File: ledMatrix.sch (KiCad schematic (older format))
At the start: 21 parts

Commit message: BIG UPDATE! omg so big
New boards and other things.. jeesh it sbeen too long since the last update
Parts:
- LED1, LED10, LED11, LED12, LED13, LED14, LED15, LED16, LED2, LED3, LED4, LED5, LED6, LED7, LED8, LED9: footprint afx-01:WS2811_5mm_ThroughHole -> Zetaohm:WS2812b_SMD
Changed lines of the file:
@@
 EESchema Schematic File Version 2
-LIBS:afx-01-rescue
+LIBS:Zetaohm
 LIBS:power
 LIBS:device
@@
 LIBS:contrib
 LIBS:valves
-LIBS:afx-01-cache
-LIBS:ZettaOhm
 EELAYER 25 0
 EELAYER END
 $Descr User 5906 5906
 encoding utf-8
-Sheet 2 5
+Sheet 2 7
 Title ""
 Date ""
@@
 F 0 "LED1" H 2750 1750 20  0000 C CNN
 F 1 "WS2812b" H 2600 1750 20  0000 C CNN
-F 2 "afx-01:WS2811_5mm_ThroughHole" H 2300 2250 60  0001 C CNN
+F 2 "Zetaohm:WS2812b_SMD" H 2300 2250 60  0001 C CNN
 F 3 "" H 2300 2250 60  0000 C CNN
 	1    2600 1500
@@
 F 0 "LED5" H 2750 2300 20  0000 C CNN
 F 1 "WS2812b" H 2600 2300 20  0000 C CNN
-F 2 "afx-01:WS2811_5mm_ThroughHole" H 2300 2800 60  0001 C CNN
+F 2 "Zetaohm:WS2812b_SMD" H 2300 2800 60  0001 C CNN
 F 3 "" H 2300 2800 60  0000 C CNN
 	1    2600 2050
@@
 F 0 "LED9" H 2750 2850 20  0000 C CNN
 F 1 "WS2812b" H 2600 2850 20  0000 C CNN
-F 2 "afx-01:WS2811_5mm_ThroughHole" H 2300 3350 60  0001 C CNN
+F 2 "Zetaohm:WS2812b_SMD" H 2300 3350 60  0001 C CNN
 F 3 "" H 2300 3350 60  0000 C CNN
 	1    2600 2600
@@
 F 0 "LED13" H 2750 3400 20  0000 C CNN
 F 1 "WS2812b" H 2600 3400 20  0000 C CNN
-F 2 "afx-01:WS2811_5mm_ThroughHole" H 2300 3900 60  0001 C CNN
+F 2 "Zetaohm:WS2812b_SMD" H 2300 3900 60  0001 C CNN
 F 3 "" H 2300 3900 60  0000 C CNN
 	1    2600 3150
@@
 F 0 "LED2" H 3250 1750 20  0000 C CNN
 F 1 "WS2812b" H 3100 1750 20  0000 C CNN
-F 2 "afx-01:WS2811_5mm_ThroughHole" H 2800 2250 60  0001 C CNN
+F 2 "Zetaohm:WS2812b_SMD" H 2800 2250 60  0001 C CNN
 F 3 "" H 2800 2250 60  0000 C CNN
 	1    3100 1500
@@
 F 0 "LED6" H 3250 2300 20  0000 C CNN
 F 1 "WS2812b" H 3100 2300 20  0000 C CNN
-F 2 "afx-01:WS2811_5mm_ThroughHole" H 2800 2800 60  0001 C CNN
+F 2 "Zetaohm:WS2812b_SMD" H 2800 2800 60  0001 C CNN
 F 3 "" H 2800 2800 60  0000 C CNN
 	1    3100 2050
@@
 F 0 "LED10" H 3250 2850 20  0000 C CNN
 F 1 "WS2812b" H 3100 2850 20  0000 C CNN
-F 2 "afx-01:WS2811_5mm_ThroughHole" H 2800 3350 60  0001 C CNN
+F 2 "Zetaohm:WS2812b_SMD" H 2800 3350 60  0001 C CNN
 F 3 "" H 2800 3350 60  0000 C CNN
 	1    3100 2600
@@
 F 0 "LED14" H 3250 3400 20  0000 C CNN
 F 1 "WS2812b" H 3100 3400 20  0000 C CNN
-F 2 "afx-01:WS2811_5mm_ThroughHole" H 2800 3900 60  0001 C CNN
+F 2 "Zetaohm:WS2812b_SMD" H 2800 3900 60  0001 C CNN
 F 3 "" H 2800 3900 60  0000 C CNN
 	1    3100 3150
@@
 F 0 "LED3" H 3750 1750 20  0000 C CNN
 F 1 "WS2812b" H 3600 1750 20  0000 C CNN
-F 2 "afx-01:WS2811_5mm_ThroughHole" H 3300 2250 60  0001 C CNN
+F 2 "Zetaohm:WS2812b_SMD" H 3300 2250 60  0001 C CNN
 F 3 "" H 3300 2250 60  0000 C CNN
 	1    3600 1500
@@
 F 0 "LED7" H 3750 2300 20  0000 C CNN
 F 1 "WS2812b" H 3600 2300 20  0000 C CNN
-F 2 "afx-01:WS2811_5mm_ThroughHole" H 3300 2800 60  0001 C CNN
+F 2 "Zetaohm:WS2812b_SMD" H 3300 2800 60  0001 C CNN
 F 3 "" H 3300 2800 60  0000 C CNN
 	1    3600 2050
@@
 F 0 "LED11" H 3750 2850 20  0000 C CNN
 F 1 "WS2812b" H 3600 2850 20  0000 C CNN
-F 2 "afx-01:WS2811_5mm_ThroughHole" H 3300 3350 60  0001 C CNN
+F 2 "Zetaohm:WS2812b_SMD" H 3300 3350 60  0001 C CNN
 F 3 "" H 3300 3350 60  0000 C CNN
 	1    3600 2600
@@
 F 0 "LED15" H 3750 3400 20  0000 C CNN
 F 1 "WS2812b" H 3600 3400 20  0000 C CNN
-F 2 "afx-01:WS2811_5mm_ThroughHole" H 3300 3900 60  0001 C CNN
+F 2 "Zetaohm:WS2812b_SMD" H 3300 3900 60  0001 C CNN
 F 3 "" H 3300 3900 60  0000 C CNN
 	1    3600 3150
@@
 F 0 "LED4" H 4250 1750 20  0000 C CNN
 F 1 "WS2812b" H 4100 1750 20  0000 C CNN
-F 2 "afx-01:WS2811_5mm_ThroughHole" H 3800 2250 60  0001 C CNN
+F 2 "Zetaohm:WS2812b_SMD" H 3800 2250 60  0001 C CNN
 F 3 "" H 3800 2250 60  0000 C CNN
 	1    4100 1500
@@
 F 0 "LED8" H 4250 2300 20  0000 C CNN
 F 1 "WS2812b" H 4100 2300 20  0000 C CNN
-F 2 "afx-01:WS2811_5mm_ThroughHole" H 3800 2800 60  0001 C CNN
+F 2 "Zetaohm:WS2812b_SMD" H 3800 2800 60  0001 C CNN
 F 3 "" H 3800 2800 60  0000 C CNN
 	1    4100 2050
@@
 F 0 "LED12" H 4250 2850 20  0000 C CNN
 F 1 "WS2812b" H 4100 2850 20  0000 C CNN
-F 2 "afx-01:WS2811_5mm_ThroughHole" H 3800 3350 60  0001 C CNN
+F 2 "Zetaohm:WS2812b_SMD" H 3800 3350 60  0001 C CNN
 F 3 "" H 3800 3350 60  0000 C CNN
 	1    4100 2600
@@
 F 0 "LED16" H 4250 3400 20  0000 C CNN
 F 1 "WS2812b" H 4100 3400 20  0000 C CNN
-F 2 "afx-01:WS2811_5mm_ThroughHole" H 3800 3900 60  0001 C CNN
+F 2 "Zetaohm:WS2812b_SMD" H 3800 3900 60  0001 C CNN
 F 3 "" H 3800 3900 60  0000 C CNN
 	1    4100 3150

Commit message: UPDATEUPDATES!!!
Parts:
- removed C1, C2, C3, C4: 100µf, Capacitors_SMD:C_0805_HandSoldering, symbol Cap
- added C1, C2, C3, C4: 100uf, symbol C_Small
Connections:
- net labels added: +3V3
- net labels removed: VCC
- wire segments 38 -> 103
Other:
- moved on the sheet: LED1, LED2, LED3, LED4, R1

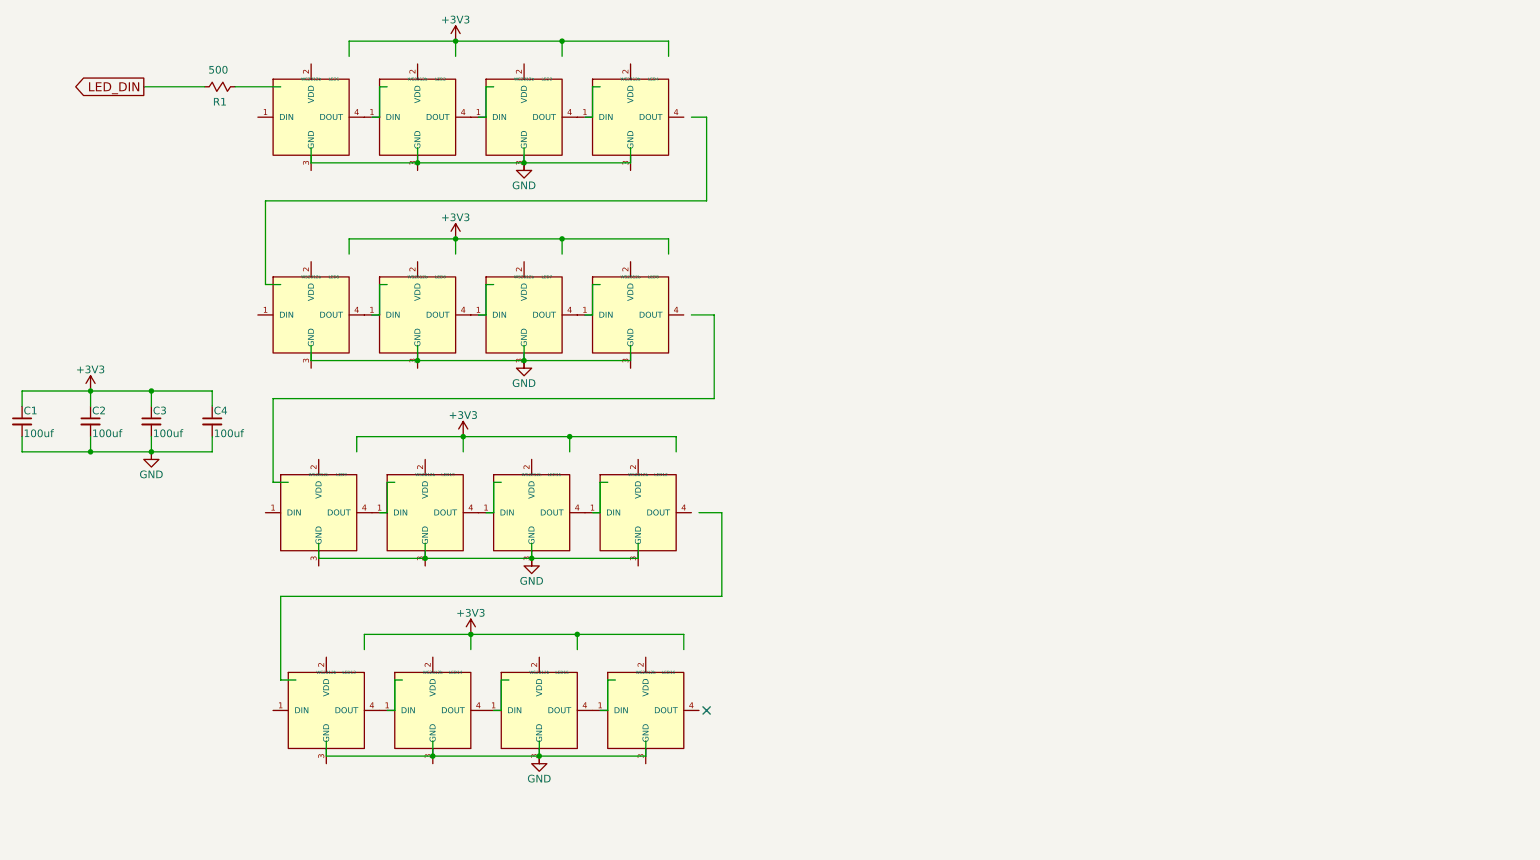
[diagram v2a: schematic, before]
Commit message: Added Touch Capacitive Panel
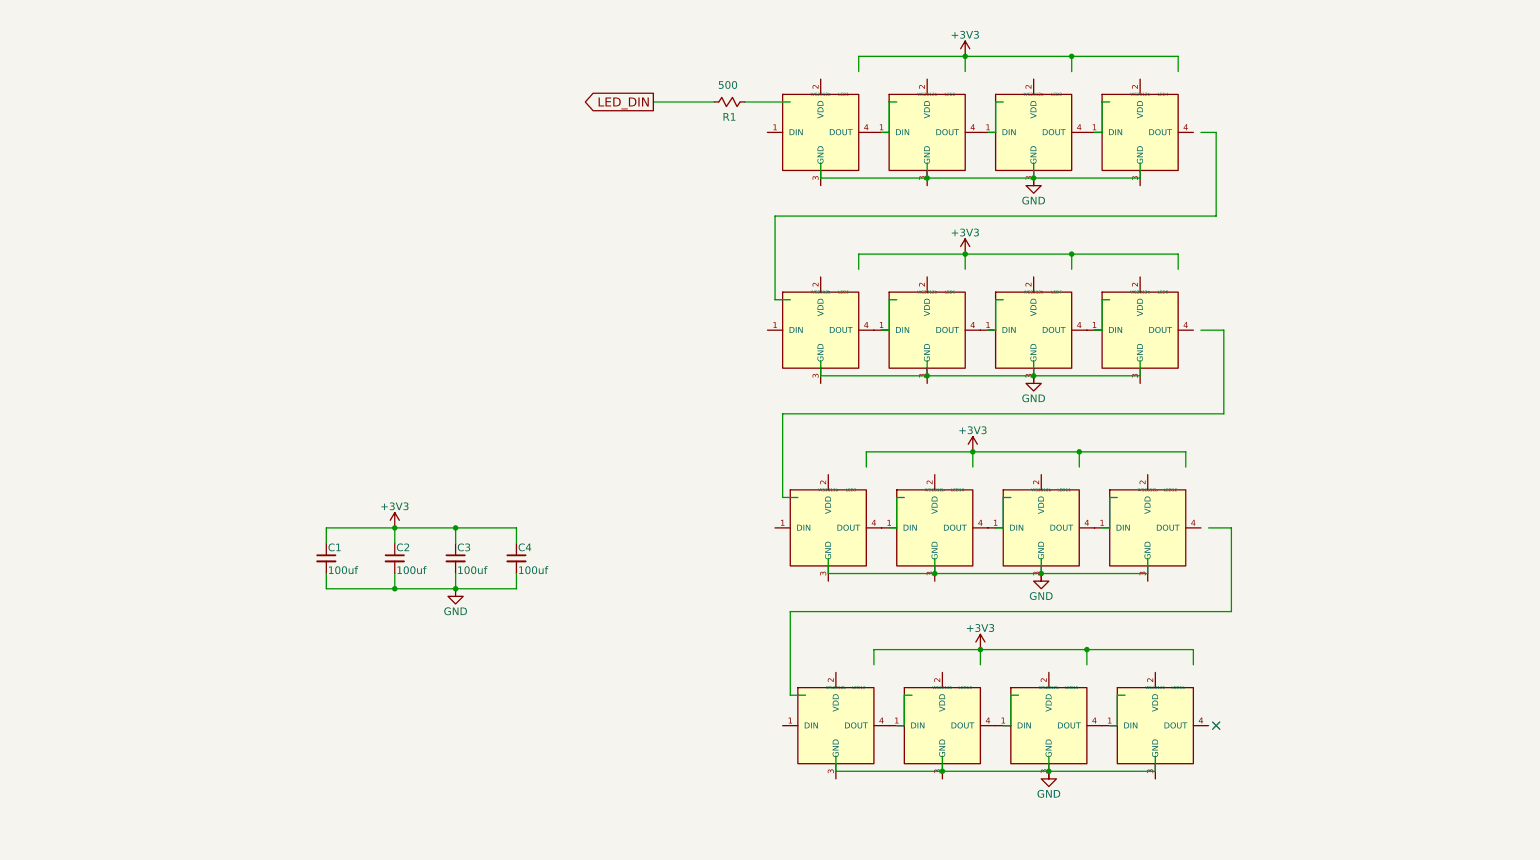
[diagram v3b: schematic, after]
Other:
- moved on the sheet: C1, C2, C3, C4, LED1, LED10, LED11, LED12, LED13, LED14, LED15, LED16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

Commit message: Updating footprints
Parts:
- C1, C2, C3, C4: footprint (none) -> Capacitors_SMD:C_0603_HandSoldering
- R1: footprint Resistors_SMD:R_0805_HandSoldering -> Resistors_SMD:R_0603_HandSoldering
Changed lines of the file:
@@
 $Descr User 11811 7874
 encoding utf-8
-Sheet 2 8
+Sheet 2 7
 Title ""
 Date ""
@@
 F 0 "R1" V 5450 1200 50  0000 C CNN
 F 1 "500" V 5240 1190 50  0000 C CNN
-F 2 "Resistors_SMD:R_0805_HandSoldering" V 5280 1200 30  0001 C CNN
+F 2 "Resistors_SMD:R_0603_HandSoldering" V 5280 1200 30  0001 C CNN
 F 3 "" H 5350 1200 30  0000 C CNN
 	1    5350 1200
@@
 F 0 "C1" H 2710 4270 50  0000 L CNN
 F 1 "100uf" H 2710 4120 50  0000 L CNN
-F 2 "" H 2700 4200 60  0000 C CNN
+F 2 "Capacitors_SMD:C_0603_HandSoldering" H 2700 4200 60  0001 C CNN
 F 3 "" H 2700 4200 60  0000 C CNN
 	1    2700 4200
@@
 F 0 "C2" H 3160 4270 50  0000 L CNN
 F 1 "100uf" H 3160 4120 50  0000 L CNN
-F 2 "" H 3150 4200 60  0000 C CNN
+F 2 "Capacitors_SMD:C_0603_HandSoldering" H 3150 4200 60  0001 C CNN
 F 3 "" H 3150 4200 60  0000 C CNN
 	1    3150 4200
@@
 F 0 "C3" H 3560 4270 50  0000 L CNN
 F 1 "100uf" H 3560 4120 50  0000 L CNN
-F 2 "" H 3550 4200 60  0000 C CNN
+F 2 "Capacitors_SMD:C_0603_HandSoldering" H 3550 4200 60  0001 C CNN
 F 3 "" H 3550 4200 60  0000 C CNN
 	1    3550 4200
@@
 F 0 "C4" H 3960 4270 50  0000 L CNN
 F 1 "100uf" H 3960 4120 50  0000 L CNN
-F 2 "" H 3950 4200 60  0000 C CNN
+F 2 "Capacitors_SMD:C_0603_HandSoldering" H 3950 4200 60  0001 C CNN
 F 3 "" H 3950 4200 60  0000 C CNN
 	1    3950 4200

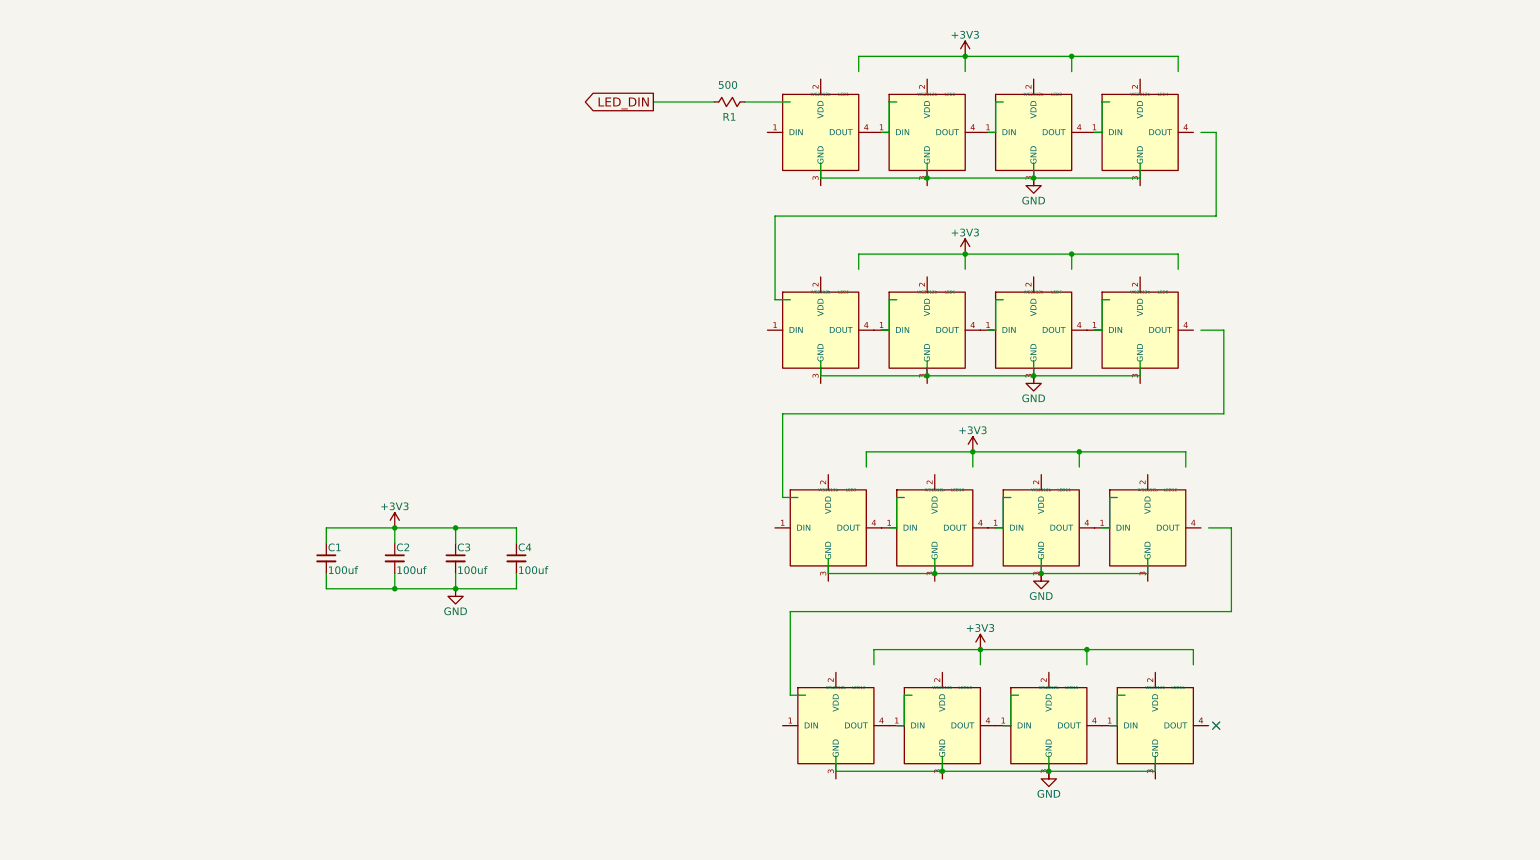
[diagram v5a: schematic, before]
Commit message: UPDATING SCHEMATIC FOR SSD1327
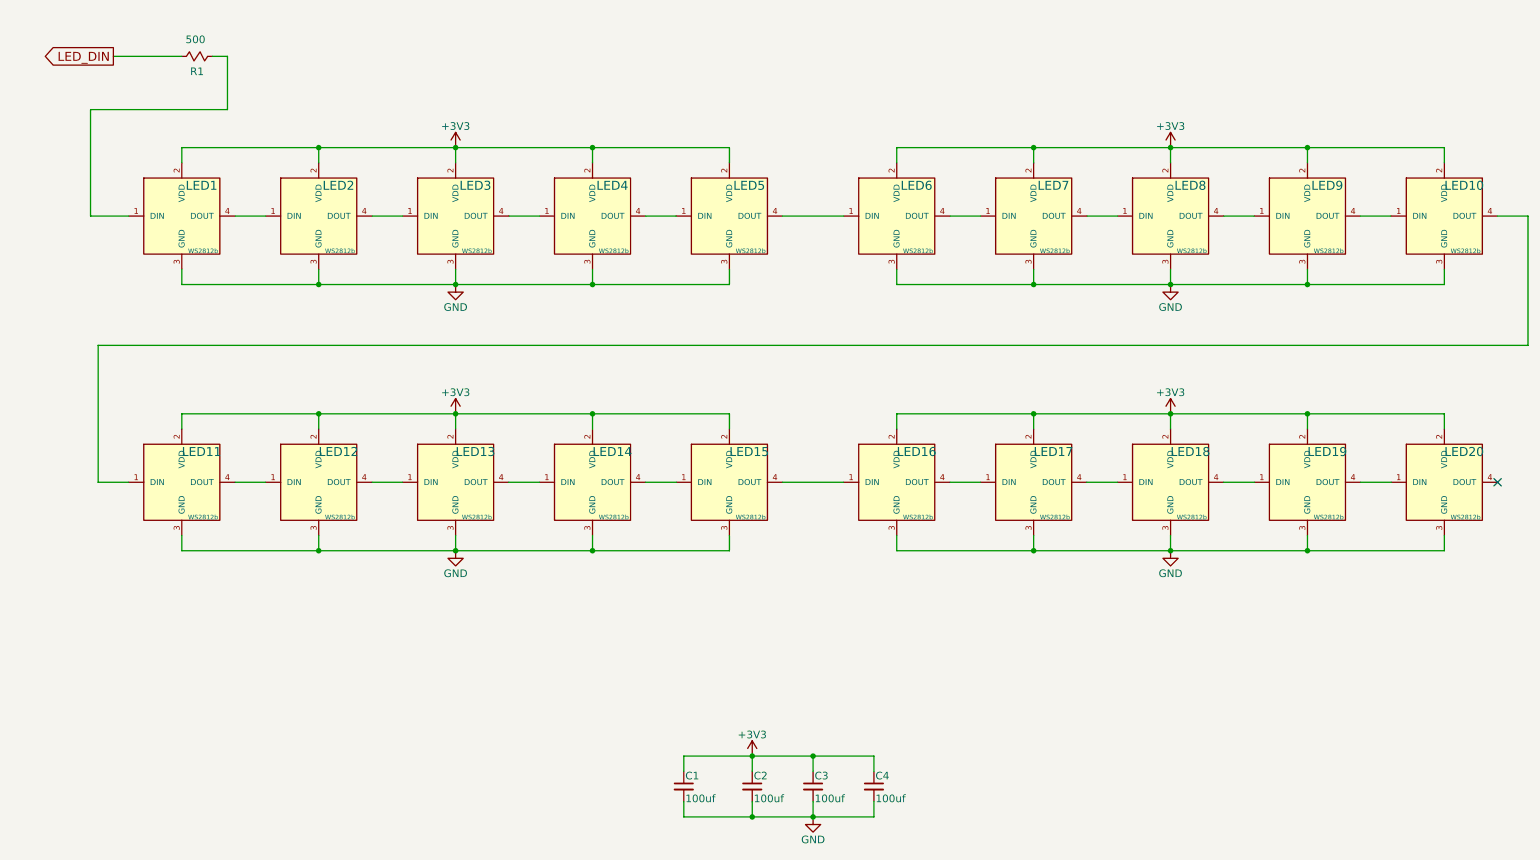
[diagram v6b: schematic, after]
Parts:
- added LED17, LED18, LED19, LED20: WS2812b, Zetaohm:WS2812b_SMD, symbol WS2812b
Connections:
- wire segments 103 -> 87
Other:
- moved on the sheet: C1, C2, C3, C4, R1
